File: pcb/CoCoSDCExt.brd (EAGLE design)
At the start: 101.6 x 31.8 mm, 47 parts, among them IC1 AM29F040J, IC2 XC9572XLVQG64, IC3 YM2413R, IC4 SN76489R, IC6 LM4558D, X1 EXPANSION_PORT_COCO, X2 EXPANSION_PORT_COCOS

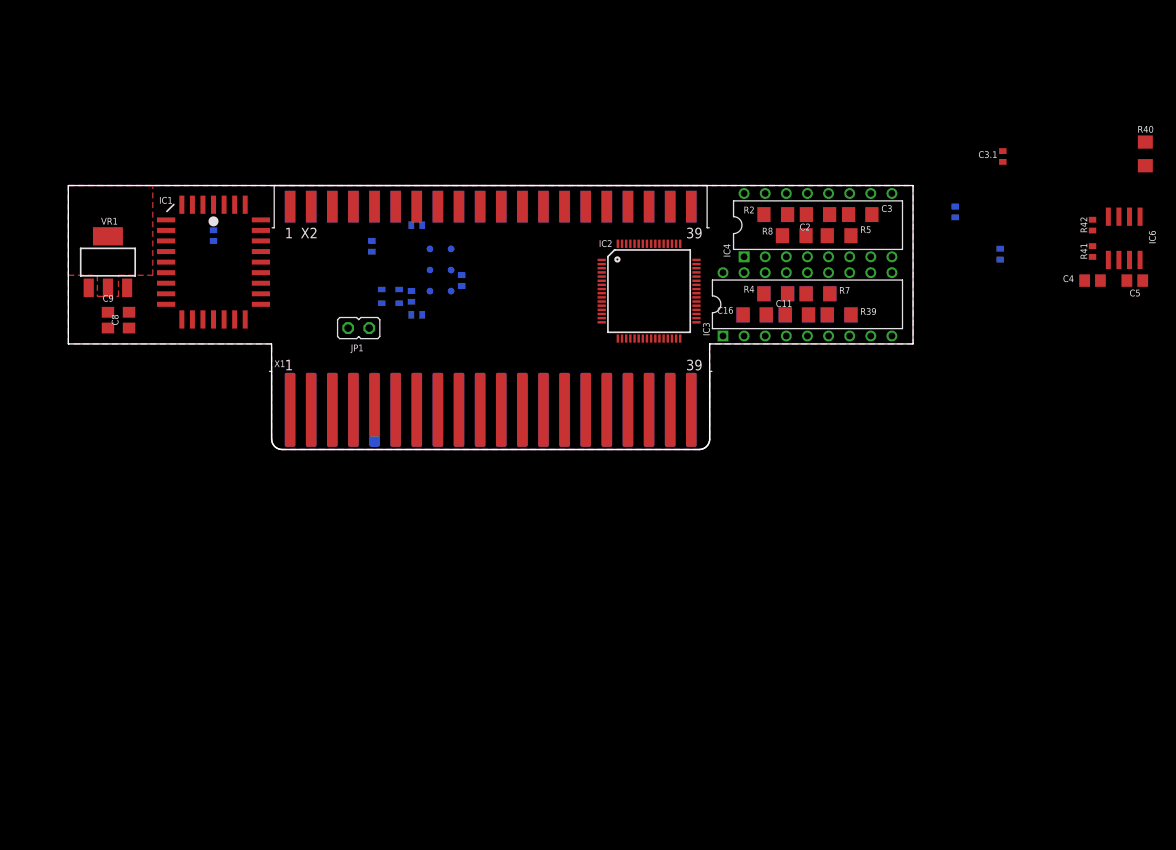
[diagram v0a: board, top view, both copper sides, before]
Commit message: Add in YMF-262 audio IC
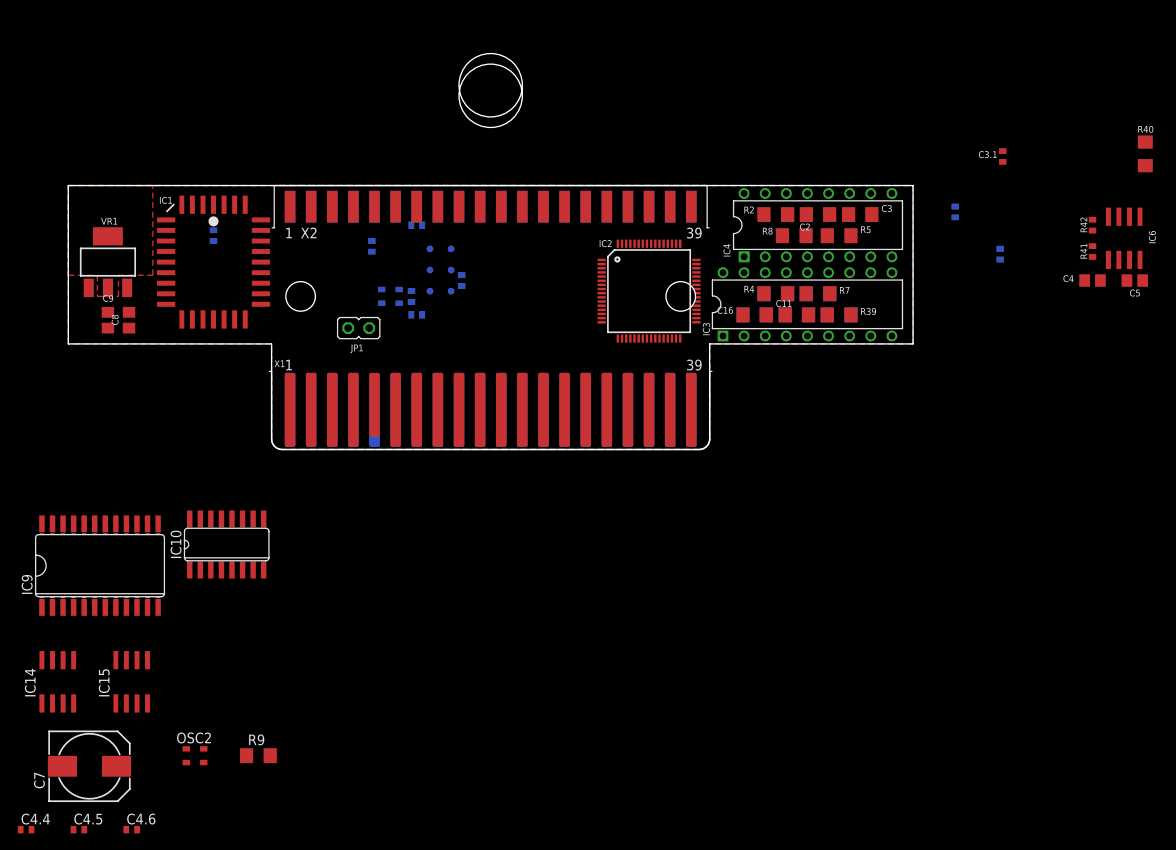
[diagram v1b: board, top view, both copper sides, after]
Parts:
- added C4.4: 50p, rcl:C0402
- added C4.5, C4.6: 2n7, rcl:C0402
- added C7: 10, rcl:140CLH-0810
- added IC10: YAC512-M, yamaha:SO16
- added IC14, IC15: TL072D, linear:SO08
- added IC9: YMF262-M, yamaha:SO24W
- added OSC2: 16MHz, crystal:ASE
- added R9: 33, resistor:R1206
- added U$1: (no value), coco:PROGRAM_PAK
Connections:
- new net !CE_YMF262: IC9.8
- new net !IRQ_AUDIO: IC9.2
- new net !OE: IC9.7
- new net !RESET_AUDIO: IC9.3
- new net AB0: IC9.4
- new net AB1: IC9.5
- new net DB0: IC9.10
- new net DB1: IC9.11
- new net DB2: IC9.13
- new net DB3: IC9.14
- new net DB4: IC9.15
- new net DB5: IC9.16
- new net DB6: IC9.17
- new net DB7: IC9.18
- new net N$10: IC10.8, IC9.20
- new net N$11: IC10.7, IC9.19
- new net N$12: IC9.24, OSC2.3
- new net N$14: IC10.12, R9.2
- new net N$18: IC15.6, IC15.7, R9.1
- new net N$19: C4.6.1, IC10.10, IC14.5
- new net N$20: C4.5.1, IC10.11, IC14.3
- new net N$23: C4.4.1, IC10.13, IC15.5
- new net N$26: IC10.14, IC15.1, IC15.2
- new net N$28: C7.+, IC10.16, IC15.3
- new net N$6: IC10.5, IC9.23
- new net N$7: IC10.4, IC9.21
- new net V+: IC14.8, IC15.8
- new net V-: IC14.4, IC15.4
- new net YMF_CH_0: IC14.6, IC14.7
- new net YMF_CH_1: IC14.1, IC14.2
- net !WE: now also IC9.6
- net +3V3: now also OSC2.4
- net +5V: now also IC10.6, IC10.9
- net GND: now also C4.4.2, C4.5.2, C4.6.2, C7.-, IC10.2, IC9.12, OSC2.2
- net VCC: now also IC10.1, IC10.3, IC9.1

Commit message: Initial fitment
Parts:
- removed C1.2, C3.1, C4.1: .1, resistor:C0402
- removed C10, C11, C2: .1, resistor:C1206
- removed C14, C16, C3: .0015, resistor:C1206
- removed C4: 10, resistor:C0805
- removed C5: 1/50, resistor:C0805
- removed IC3: YM2413R, yamaha:DIL18-RP
- removed IC4: SN76489R, texas-instruments:DIL16-RP
- removed IC6: LM4558D, op-amps-jlb:SO08
- removed OSC2: 16MHz, crystal:ASE
- removed R1: 10K, resistor:R0402
- removed R2, R38, R39: 10K, rcl:R1206
- removed R3, R4, R5: 4K7, rcl:R1206
- removed R40: 16K, rcl:R1206
- removed R41: 1.3K (1%), rcl:R0402
- removed R42: 1k (1%), rcl:R0402
- removed R6, R7, R8: 2K2, rcl:R1206
- added C10.1, C14.1, C15.1, C15.2, C9.1: .1, rcl:C0402
- added C17, C18, C19, C20: (no value), cap-pan40:SV-B
- added C4.2: 10u, rcl:C0402
- added R10, R11: 2K, resistor:R1206
- added R12, R13: 10K, resistor:R1206
- added R14, R15: 10K, resistor:R0402
- added R16: ?K, resistor:R1206
- added SV1: (no value), con-lstb-rp:MA03-1
- C7: value 10 -> (none); device rcl:140CLH-0810 -> cap-pan40:SV-B
- IC14, IC15: value TL072D -> TL974; device linear:SO08 -> linear-jlb:TSSOP14
- OSC1: value ASE -> 16MHz
- R9: device resistor:R1206 -> resistor:R0402
- moved C4.4 123.3 mm to (45.7, 24.1), flipped to the bottom, turned to 90 degrees
- moved C4.5 116.5 mm to (43.2, 24.8), flipped to the bottom, turned to 90 degrees
- moved C4.6 110.5 mm to (41.9, 24.8), flipped to the bottom, turned to 90 degrees
- moved IC14 104.7 mm to (42.5, 16.8)
- moved IC15 101.5 mm to (47.9, 16.8)
- moved R9 92.4 mm to (44.5, 20.6), turned to 90 degrees
- moved C7 88.5 mm to (20.3, 17.8), turned to 270 degrees
- moved IC9 88.1 mm to (33.0, 22.9), turned to 270 degrees
- moved IC10 85.8 mm to (45.1, 26.7), turned to 180 degrees
- moved OSC1 47.0 mm to (33.7, 29.2), turned to 90 degrees
- moved C1.1 21.8 mm to (43.5, 36.2)
- moved IC2 8.89 mm to (10.2, 19.1)
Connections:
- removed net CH0: IC3.15, R3.2, R6.1
- removed net CH1: IC3.14, R4.2, R7.1
- removed net N$1: C10.1, C14.1, R3.1
- removed net N$2: C2.1, R2.2
- removed net N$3: IC6.2, R2.1, R38.1, R39.1, R40.2
- removed net N$4: C11.2, C16.1, R4.1
- removed net N$49: C10.2, R38.2
- removed net N$5: C2.2, C3.1, R5.1
- removed net N$50: C11.1, R39.2
- removed net N$52: IC6.3, IC6.6, IC6.7
- removed net N$54: C5.1, IC6.1, R40.1
- removed net N$55: C4.1, IC6.5, R41.1, R42.2
- removed net N$8: IC2.15, OSC1.3
- removed net V+: IC14.8, IC15.8
- removed net V-: IC14.4, IC15.4
- new net AUDIO_L: C7.+, SV1.1
- new net AUDIO_R: C18.+, SV1.3
- new net N$13: C18.-, C19.-, R11.1
- new net N$15: C17.+, R12.2
- new net N$16: C19.+, R13.2
- new net N$17: IC15.6, R12.1, R13.1, R16.2
- new net N$21: IC15.1, IC15.2, IC15.5
- new net N$24: C15.2.1, IC15.3, R14.2, R15.1
- new net N$27: C20.-, IC15.7, R16.1
- new net N$9: C17.-, C7.-, R10.1
- net !CE_SN: no longer IC4.6
- net !CE_YM: no longer IC3.12
- net !RESET_YM: no longer IC3.13
- net !WE_SN: no longer IC4.5
- net +3V3: no longer C1.2.1, OSC2.4
- net +5V: now also C10.1.1, C14.1.1, C15.1.1, C9.1.1, IC10.1, IC10.3, IC14.4, IC15.4, IC9.1, R14.1; no longer C3.1.1, C4.1.1, IC3.16, IC4.16, IC6.8, R1.2, R42.1
- net A0_YM: no longer IC3.10
- net BD0: no longer IC4.10
- net BD1: no longer IC4.11
- net BD2: no longer IC4.12
- net BD3: no longer IC4.13
- net BD4: no longer IC4.15
- net BD5: no longer IC4.1
- net BD6: no longer IC4.2
- net BD7: no longer IC4.3
- net CH2: no longer IC4.7, R5.2, R8.1
- net CLK_SN: no longer IC4.14
- net CLK_YM: no longer IC3.8
- net D0: no longer IC3.17
- net D1: no longer IC3.18
- net D2: no longer IC3.2
- net D3: no longer IC3.3
- net D4: no longer IC3.4
- net D5: no longer IC3.5
- net D6: no longer IC3.6
- net D7: no longer IC3.7
- net GND: now also C10.1.2, C14.1.2, C15.1.2, C15.2.2, C4.2.2, C9.1.2, IC14.11, IC15.11, R15.2, SV1.2; no longer C1.2.2, C14.2, C16.2, C3.1.2, C3.2, C4.1.2, C4.2, C7.-, IC3.1, IC3.11, IC4.8, IC6.4, OSC2.2, R41.2, R6.2, R7.2, R8.2
- net N$12: now also OSC1.3; no longer OSC2.3
- net N$18: now also IC14.13, IC14.14; no longer IC15.6, IC15.7
- net N$23: now also IC14.12; no longer IC15.5
- net N$26: now also IC14.8, IC14.9; no longer IC15.1, IC15.2
- net N$28: now also C4.2.1, IC14.10; no longer C7.+, IC15.3
- net READY: no longer IC4.4, R1.1
- net SND: now also C20.+; no longer C5.2
- net VCC: no longer IC10.1, IC10.3, IC9.1
- net YMF_CH_0: now also R10.2
- net YMF_CH_1: now also R11.2

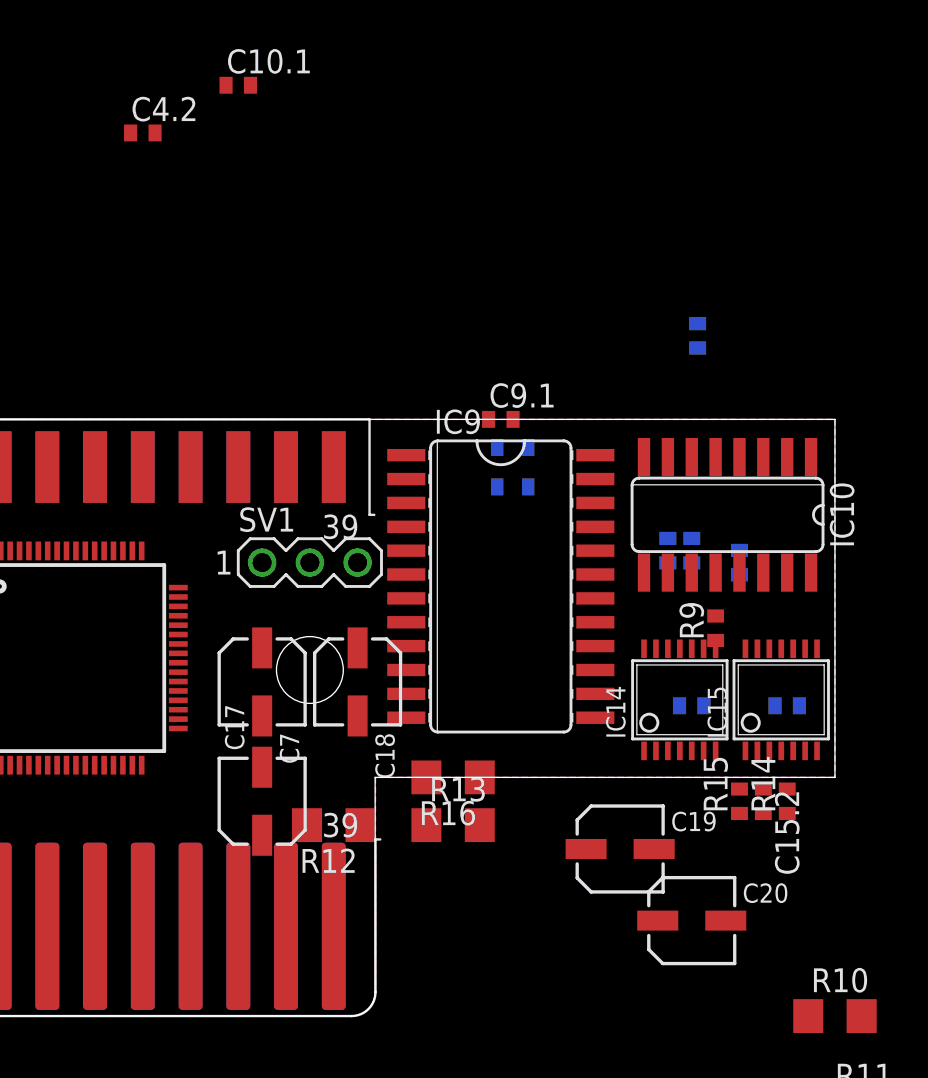
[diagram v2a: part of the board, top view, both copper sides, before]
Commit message: More fitment positioning
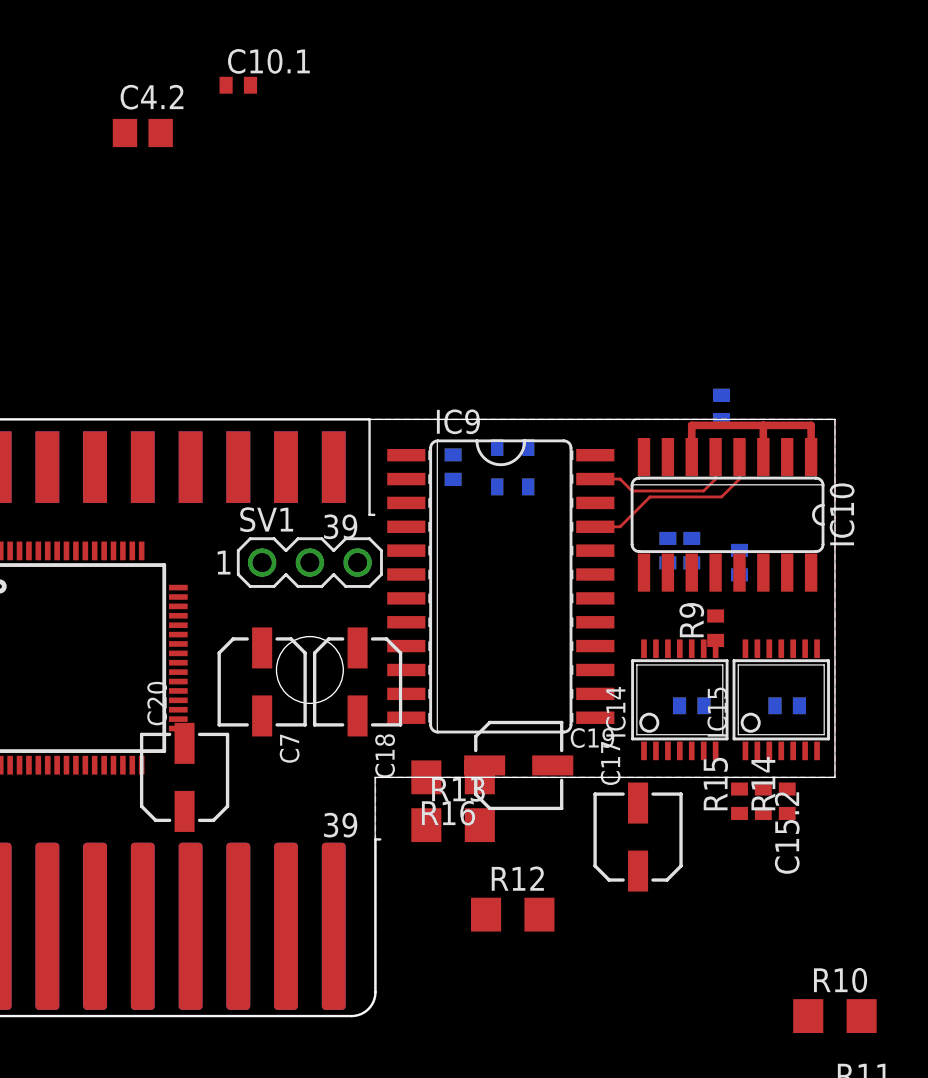
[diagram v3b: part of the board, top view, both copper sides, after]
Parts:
- C4.2: device rcl:C0402 -> rcl:C0805
- moved C20 28.0 mm to (16.2, 12.7), turned to 90 degrees
- moved C17 20.1 mm to (40.3, 9.53)
- moved R12 10.6 mm to (33.7, 5.40), turned to 0 degrees
- moved C19 6.99 mm to (34.0, 13.3)
- moved C1.1 4.02 mm to (44.8, 32.4)
- moved C9.1 3.59 mm to (30.5, 29.2), flipped to the bottom, turned to 270 degrees
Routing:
- net +5V: track 0.00 -> 11.4 mm
- net N$7: track 0.00 -> 9.89 mm
- net N$6: track 0.00 -> 8.10 mm

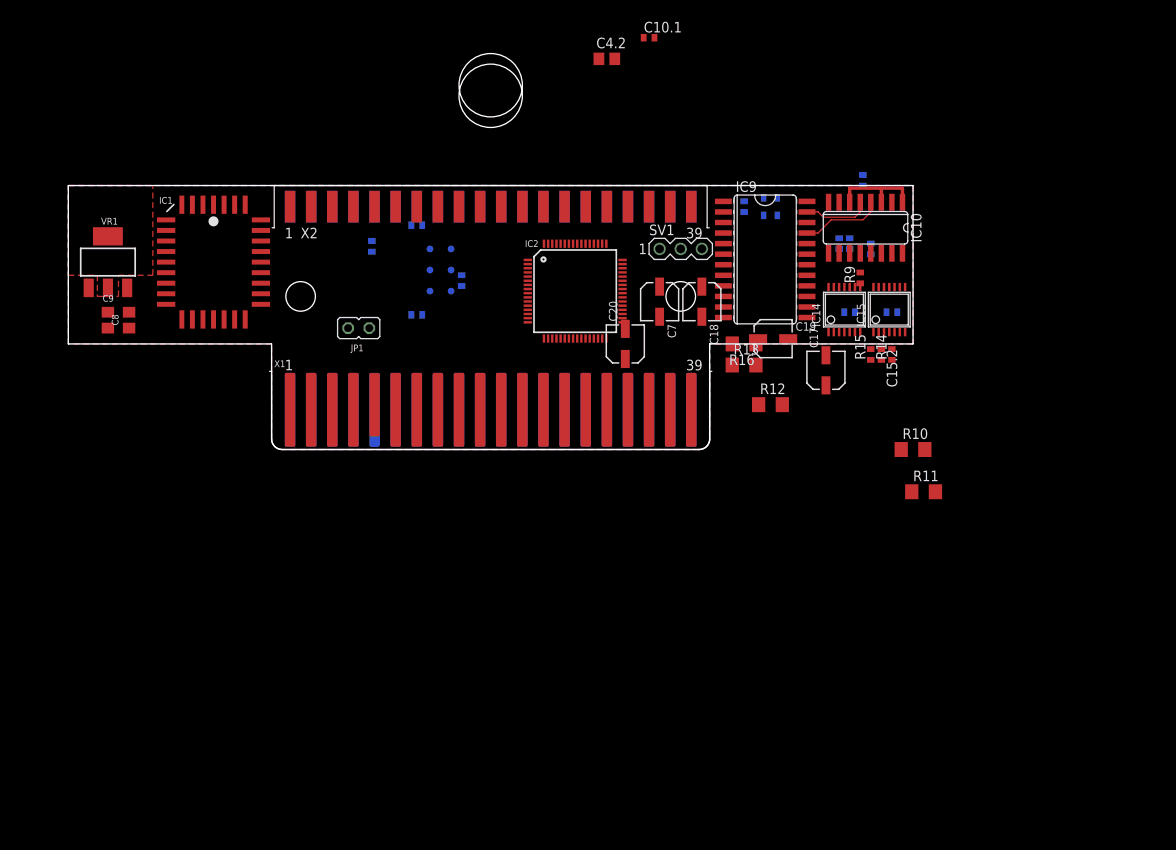
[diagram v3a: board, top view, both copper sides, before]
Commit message: Decision to use tabs below PCB for filters
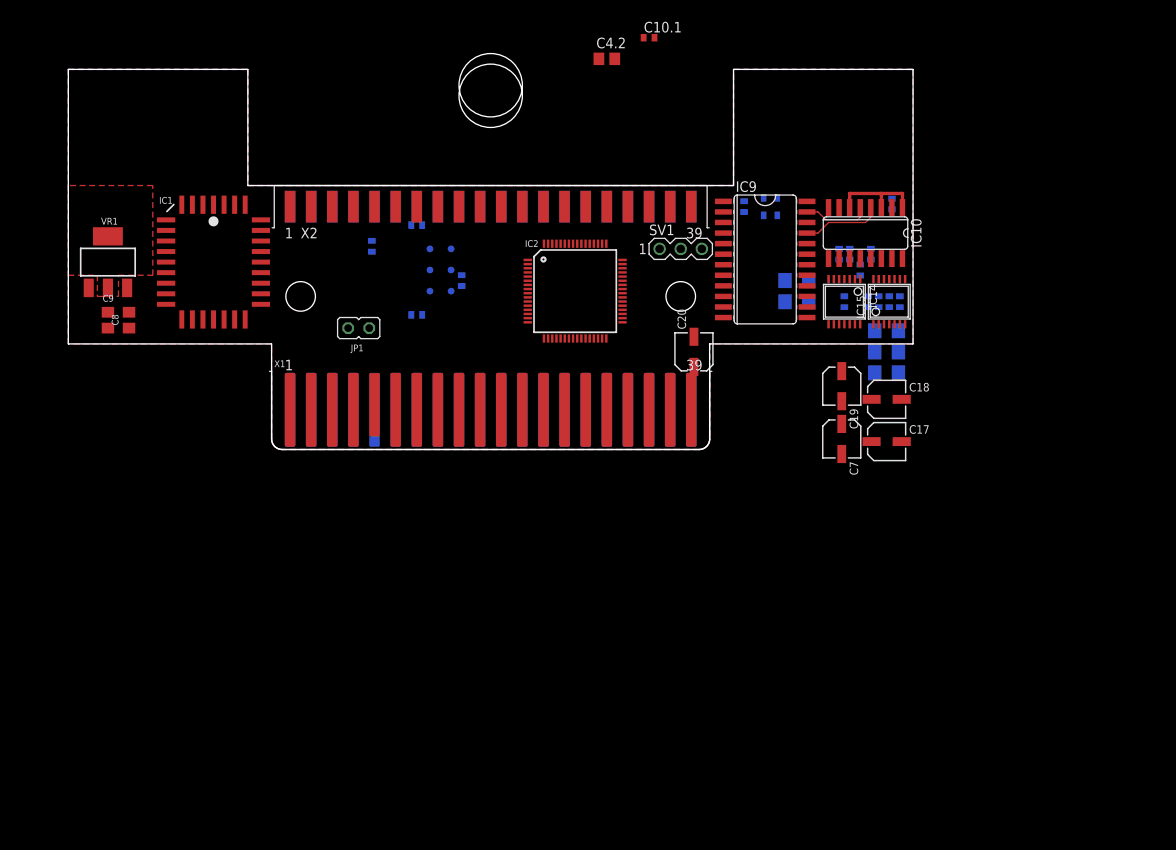
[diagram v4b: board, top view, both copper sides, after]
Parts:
- moved R11 27.5 mm to (36.8, 17.8), flipped to the bottom, turned to 180 degrees
- moved C7 27.4 mm to (42.2, 1.27)
- moved C18 25.1 mm to (47.6, 6.03), turned to 0 degrees
- moved R10 24.7 mm to (36.8, 20.3), flipped to the bottom, turned to 180 degrees
- moved R13 17.2 mm to (47.6, 11.7), flipped to the bottom
- moved R16 17.2 mm to (47.6, 14.3), flipped to the bottom
- moved R12 14.5 mm to (47.6, 9.21), flipped to the bottom
- moved C17 11.3 mm to (47.6, 0.95), turned to 0 degrees
- moved C19 10.0 mm to (42.2, 7.62), turned to 270 degrees
- moved C20 8.31 mm to (24.4, 11.7)
- moved C15.2 6.36 mm to (46.7, 17.8), flipped to the bottom, turned to 90 degrees
- moved R14 6.36 mm to (47.9, 17.8), flipped to the bottom, turned to 270 degrees
- moved R15 6.36 mm to (45.4, 17.8), flipped to the bottom
- moved C1.1 4.51 mm to (48.3, 29.5)
- moved C14.1 1.59 mm to (49.2, 17.8), turned to 90 degrees
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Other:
- board size 101.6 x 31.8 mm -> 101.6 x 45.7 mm

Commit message: positioning
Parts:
- moved C4.2 44.1 mm to (42.5, 13.3)
- moved SV1 36.9 mm to (47.0, -3.81)
- moved OSC1 1.85 mm to (35.2, 28.3)
- moved R13 1.59 mm to (47.6, 13.3)
- moved R16 1.27 mm to (47.6, 15.6)
- moved C1.1 0.71 mm to (48.9, 29.2), turned to 0 degrees
- moved R9 0.64 mm to (44.5, 22.2)
- turned C15.1 to 90 degrees
- turned IC14 to 0 degrees
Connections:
- net N$18: now also IC14.1, IC14.2; no longer IC14.13, IC14.14
- net N$19: now also IC14.12; no longer IC14.5
- net N$20: now also IC14.10; no longer IC14.3
- net N$23: now also IC14.3; no longer IC14.12
- net N$26: now also IC14.6, IC14.7; no longer IC14.8, IC14.9
- net N$28: now also IC14.5; no longer IC14.10
- net YMF_CH_0: now also IC14.13, IC14.14; no longer IC14.6, IC14.7
- net YMF_CH_1: now also IC14.8, IC14.9; no longer IC14.1, IC14.2
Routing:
- net N$28: track 0.00 -> 11.8 mm, vias 0 -> 2
- net N$26: track 0.00 -> 9.96 mm
- net N$23: track 0.00 -> 9.86 mm, vias 0 -> 1
- net N$11: track 0.00 -> 8.00 mm, vias 0 -> 2
- net N$18: track 0.00 -> 7.83 mm, vias 0 -> 1
- net +5V: track 11.4 -> 18.0 mm, vias 0 -> 3
- net N$10: track 0.00 -> 6.21 mm, vias 0 -> 2
- net N$24: track 0.00 -> 4.64 mm, vias 0 -> 1
- net N$20: track 0.00 -> 2.48 mm, vias 0 -> 1
- net N$19: track 0.00 -> 2.48 mm, vias 0 -> 1
- net YMF_CH_1: track 0.00 -> 0.64 mm
- net N$14: track 0.00 -> 0.12 mm, vias 0 -> 1

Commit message: Extending PCB to support tabs
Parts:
- C15.2: value .1 -> .1u
- C17, C18, C19, C20, C7: value (none) -> 1u
- moved R11 17.1 mm to (48.3, 5.08), turned to 270 degrees
- moved R10 16.5 mm to (43.2, 5.08), turned to 270 degrees
- moved C20 12.7 mm to (20.6, 23.8), turned to 0 degrees
- moved C17 11.1 mm to (43.2, 11.1), turned to 270 degrees
- moved C4.2 8.45 mm to (47.3, 20.3), flipped to the bottom, turned to 180 degrees
- moved C19 6.97 mm to (48.3, 11.1)
- moved R12 4.84 mm to (43.2, 11.1), turned to 90 degrees
- moved SV1 4.02 mm to (45.7, 0.00)
- moved C7 3.93 mm to (43.2, 5.08), turned to 90 degrees
- moved R13 2.31 mm to (48.3, 11.1), turned to 90 degrees
- moved C18 1.14 mm to (48.3, 5.08), turned to 90 degrees
- moved R16 1.00 mm to (47.3, 14.6)
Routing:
- net YMF_CH_0: track 0.00 -> 19.1 mm, vias 0 -> 1
- net YMF_CH_1: track 0.64 -> 19.3 mm, vias 0 -> 3
- net N$17: track 0.00 -> 11.7 mm, vias 0 -> 1
- net N$27: track 0.00 -> 6.22 mm, vias 0 -> 1
- net N$21: track 0.00 -> 3.72 mm
- net AUDIO_R: track 0.00 -> 3.27 mm
- net AUDIO_L: track 0.00 -> 3.27 mm
- net N$9: track 0.00 -> 2.41 mm
- net N$13: track 0.00 -> 2.41 mm
- net N$18: track 7.83 -> 8.46 mm
- net N$23: track 9.86 -> 10.4 mm
- net N$16: track 0.00 -> 0.39 mm, vias 0 -> 1
- net N$15: track 0.00 -> 0.39 mm, vias 0 -> 1
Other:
- board size 101.6 x 45.7 mm -> 101.6 x 47 mm
